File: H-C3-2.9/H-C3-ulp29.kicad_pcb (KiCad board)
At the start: 4 copper layers, 83.4 x 42.1 mm, 55 parts, among them CN1 HX JN1.27-2X5 TP H4.9, J1 USB_C_Receptacle_USB2.0, J2 AFC24-S24FIC-00, J4 SM04B-SRSS-TB_LF__SN_, Q1 Si1308, Q2 Si2301CDS, SW1 K2-1806SQ-A2DW-04, SW2 K2-1806SQ-A2DW-04, SW3 K2-1806SQ-A2DW-04, U1 E73-2G4M08S1C, U2 MCP1700-3302E_SOT23, U8 PCF8563T, Y1 Crystal_Small, Y2 RTC_Crystal_32MHz

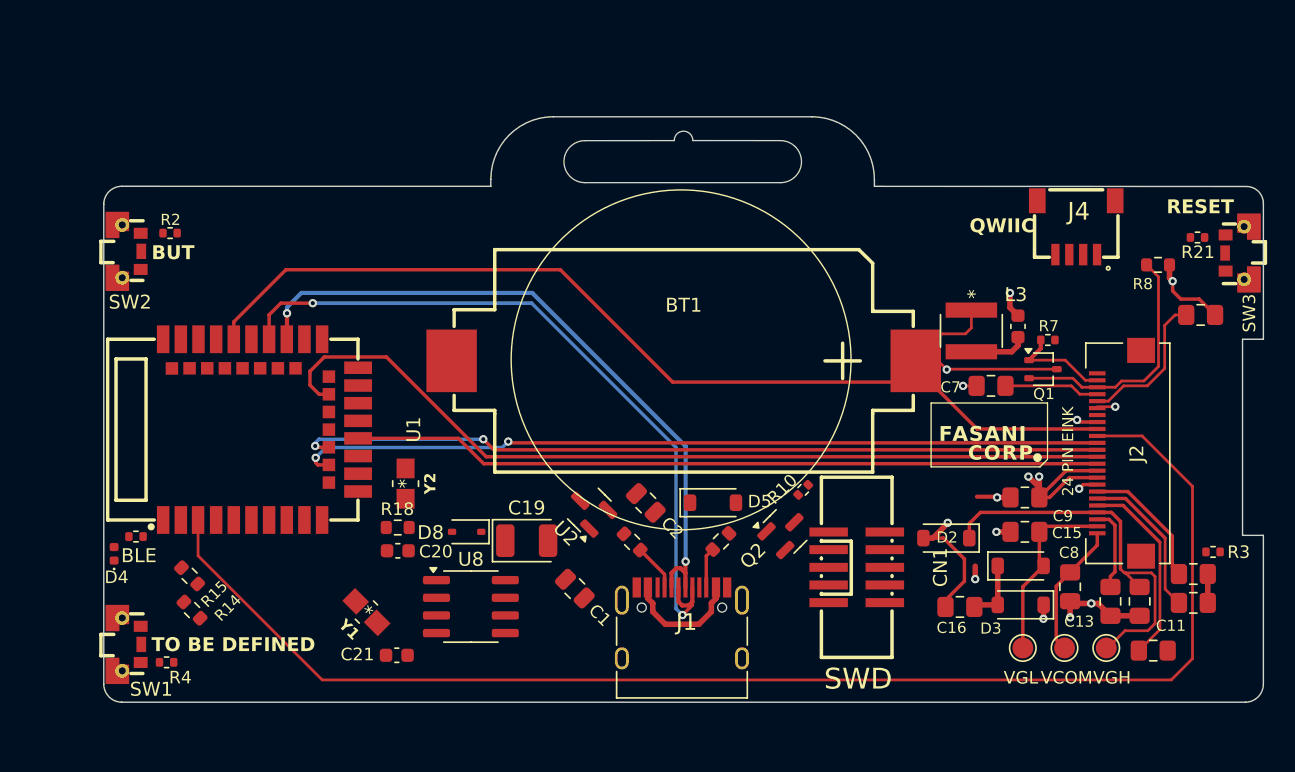
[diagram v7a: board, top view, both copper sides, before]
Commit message: Placing new knob
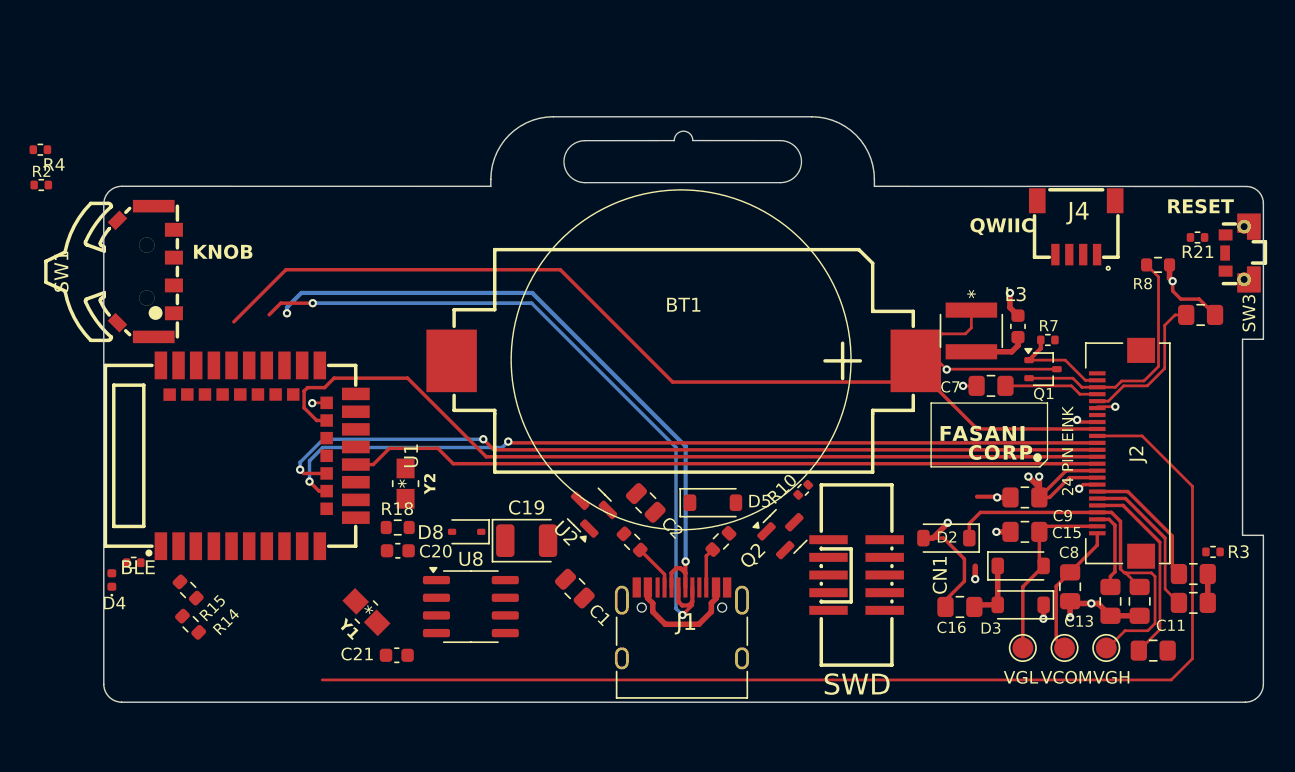
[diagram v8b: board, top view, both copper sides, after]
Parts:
- removed SW2: K2-1806SQ-A2DW-04, footprints:KEY-SMD_K2-1806SQ-A3DW-04
- R2, R4: value 10k -> 1k
- SW1: value K2-1806SQ-A2DW-04 -> TM-2023; footprint footprints:KEY-SMD_K2-1806SQ-A3DW-04 -> footprints:C318951_TM-2023-1
- moved R4 38.0 mm to (81.5, 41.9)
- moved SW1 26.8 mm to (89.1, 50.6)
- moved R2 9.89 mm to (81.6, 44.4)
- moved D4 1.89 mm to (86.7, 72.8)
- moved U1 1.89 mm to (97.2, 63.9)
- moved R5 1.89 mm to (88.3, 71.6)
- moved R14 1.02 mm to (92.3, 76.0)
- moved R15 1.02 mm to (92.2, 73.5)
- moved CN1 0.55 mm to (140.2, 72.5)
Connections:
- D5 pad 2: +5V -> +VBUS
- J1 pad A4: +5V -> +VBUS
- J1 pad A9: +5V -> +VBUS
- J1 pad B4: +5V -> +VBUS
- J1 pad B9: +5V -> +VBUS
- Q2 pad 1: +5V -> +VBUS
- R10 pad 2: +5V -> +VBUS
- SW1 pad 2: Net-(R4-Pad2) -> SW2
- SW1 pad 3: unconnected-(SW1-Pad3) -> Net-(R4-Pad2)
- SW1 pad 4: unconnected-(SW1-Pad4) -> Net-(R4-Pad2)
- SW1 pad 5: unconnected-(SW1-Pad5) -> Net-(R4-Pad2)
- U1 pad 27: unconnected-(U1-VBS-Pad27) -> +VBUS
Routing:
- net /EPD_RST: track 99.2 -> 84.0 mm
- net +VBUS: track 0.00 -> 8.73 mm
- net +5V: track 8.73 -> 0.00 mm
- net /EPD_CS: track 57.9 -> 60.9 mm
- net /EPD_DC: track 58.1 -> 60.3 mm
- net /USB_D-: track 48.5 -> 46.6 mm
- net /USB_D+: track 52.4 -> 50.7 mm
- net /EPD_BUSY: track 69.6 -> 68.4 mm
- net GND: track 26.7 -> 27.7 mm, vias 11 -> 12
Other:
- board text added: "KNOB"
- board text removed: "BUT"
- board text removed: "TO BE DEFINED"
